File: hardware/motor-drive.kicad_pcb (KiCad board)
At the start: 2 copper layers, 24 parts, among them J1 USB_C_Receptacle_USB2.0_14P, J2 Debug, SW1 RESET, SW2 BOOT, U1 STM32F405RGTx, Y1 8MHz

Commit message: MCU layout
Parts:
- moved C12 38.4 mm to (128.8, 88.0)
- moved R2 37.5 mm to (151.2, 79.6), turned to 180 degrees
- moved C13 36.6 mm to (153.3, 79.6), turned to 180 degrees
- moved J2 35.9 mm to (140.9, 79.7), turned to -90 degrees
- moved L1 35.6 mm to (128.3, 95.7)
- moved C7 35.6 mm to (135.2, 83.9)
- moved C3 34.9 mm to (135.2, 85.0)
- moved C11 33.8 mm to (128.8, 93.5), turned to 180 degrees
- moved Y1 33.1 mm to (128.8, 90.8), turned to -90 degrees
- moved C4 31.7 mm to (144.8, 86.9), turned to 90 degrees
- moved C8 29.3 mm to (145.9, 87.9), turned to 90 degrees
- moved C2 28.3 mm to (129.9, 95.6), turned to -90 degrees
- moved R3 26.5 mm to (147.1, 87.9), turned to 90 degrees
- moved C1 26.2 mm to (131.0, 95.6), turned to -90 degrees
- moved R4 24.3 mm to (147.1, 93.0), turned to -90 degrees
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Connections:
- C13 pad 1: /mcu/BOOT -> +3.3V
- C13 pad 2: GND -> /mcu/BOOT
- C3 pad 1: Net-(C3-Pad1) -> +3.3V
- C4 pad 1: Net-(C3-Pad1) -> +3.3V
- C5 pad 1: Net-(C3-Pad1) -> +3.3V
- C6 pad 1: Net-(C3-Pad1) -> +3.3V
- C7 pad 1: Net-(C3-Pad1) -> +3.3V
- J1 pad A4: VBUS -> unconnected-(J1-VBUS-PadA4)_1
- J1 pad A9: VBUS -> unconnected-(J1-VBUS-PadA4)
- J1 pad B4: VBUS -> unconnected-(J1-VBUS-PadA4)_2
- J1 pad B9: VBUS -> unconnected-(J1-VBUS-PadA4)_3
- J2 pad 1: unconnected-(J2-VTref-Pad1) -> +3.3V
- L1 pad 1: unconnected-(L1-Pad1) -> +3.3V
- R1 pad 1: unconnected-(R1-Pad1) -> +3.3V
- SW2 pad 2: unconnected-(SW2-Pad2) -> +3.3V
- U1 pad 1: Net-(U1-VBAT) -> +3.3V
- U1 pad 13: Net-(U1-VBAT) -> /mcu/VDDA
- U1 pad 19: Net-(U1-VBAT) -> +3.3V
- U1 pad 32: Net-(U1-VBAT) -> +3.3V
- U1 pad 48: Net-(U1-VBAT) -> +3.3V
- U1 pad 64: Net-(U1-VBAT) -> +3.3V
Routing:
- net +3.3V: track 0.00 -> 18.9 mm, vias 0 -> 8
- net /mcu/RESET: track 0.00 -> 17.7 mm, vias 0 -> 2
- net /mcu/SWIO: track 0.00 -> 9.16 mm
- net /USB_DN: track 0.00 -> 7.46 mm
- net /USB_DP: track 0.00 -> 7.38 mm
- net Net-(U1-PH0): track 0.00 -> 7.23 mm
- net /mcu/TDI: track 0.00 -> 6.40 mm, vias 0 -> 2
- net /mcu/SWO: track 0.00 -> 5.86 mm
- net Net-(U1-PH1): track 0.00 -> 5.34 mm
- net /mcu/SWCLK: track 0.00 -> 5.21 mm
- net /mcu/VDDA: track 0.00 -> 4.48 mm
- net /mcu/BOOT: track 0.00 -> 4.32 mm
- net Net-(J1-CC1): track 0.00 -> 2.54 mm
- net Net-(U1-VCAP_2): track 0.00 -> 2.03 mm
- net Net-(J1-CC2): track 0.00 -> 1.94 mm
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- added copper zone on B.Cu, net GND
- added copper zone on F.Cu, net GND
- added copper zone on In1.Cu, net GND
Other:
- copper layers 2 -> 4

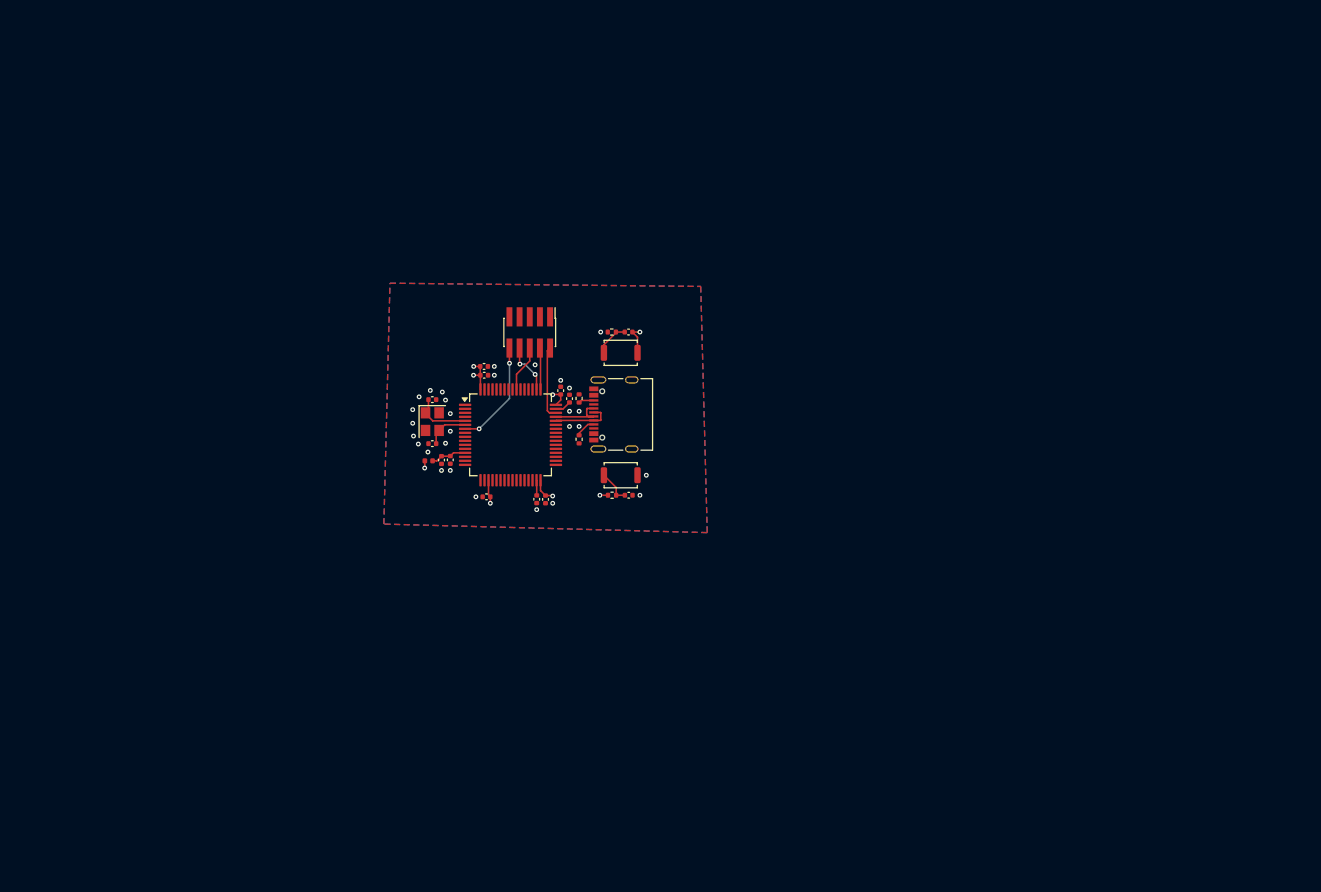
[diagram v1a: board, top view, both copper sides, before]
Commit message: Added power connector
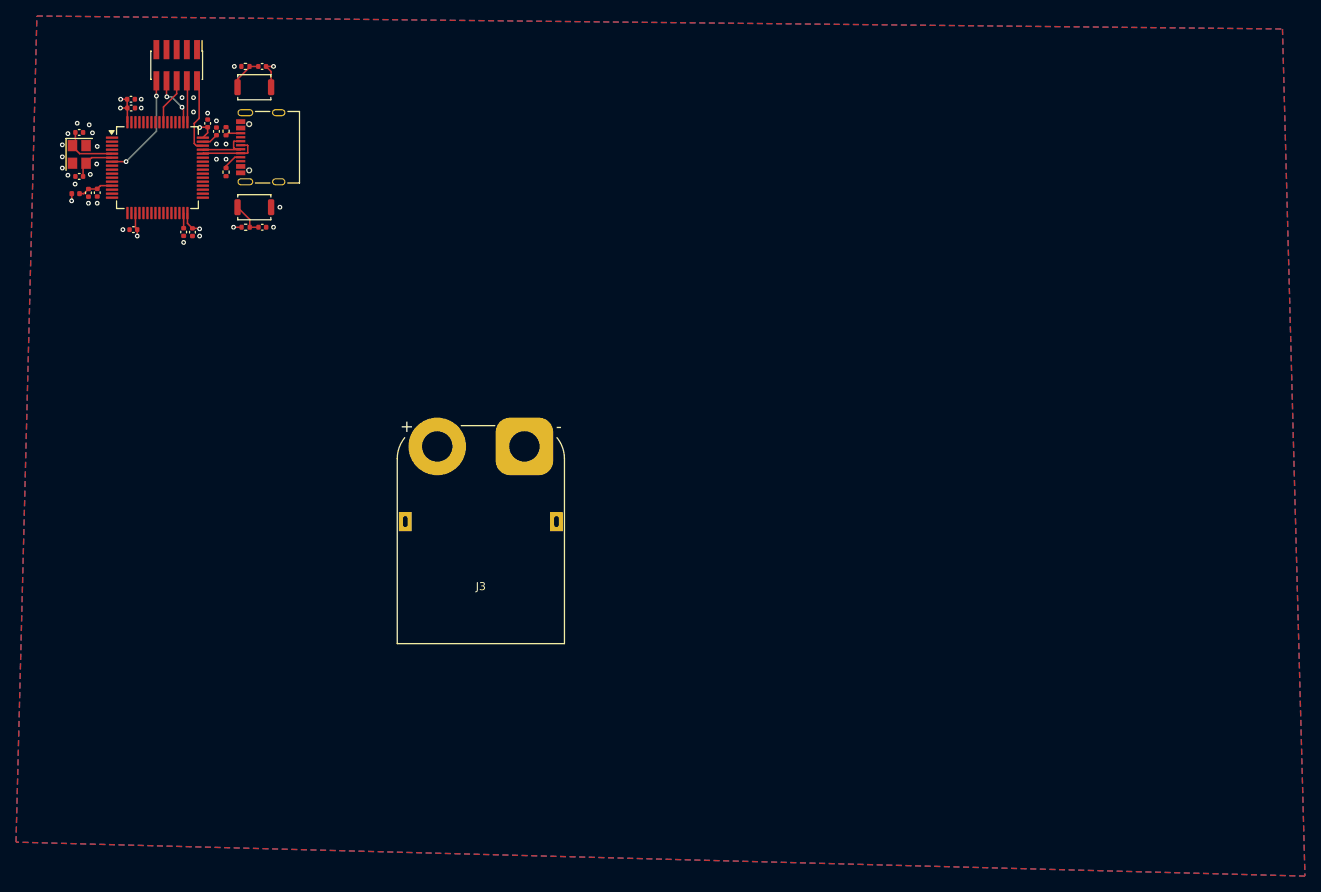
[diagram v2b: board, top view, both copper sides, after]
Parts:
- added J3: BAT, Connector_AMASS:AMASS_XT90PW-M_1x02_P10.90mm_Horizontal, F.Cu at (140.3, 93.9)
- moved C10 56.7 mm to (107.5, 66.5)
- moved SW1 56.7 mm to (106.5, 64.0)
- moved R1 56.7 mm to (105.4, 66.5)
- moved SW2 56.6 mm to (106.5, 49.0)
- moved C13 56.6 mm to (107.5, 46.4)
- moved R2 56.6 mm to (105.4, 46.4)
- moved C3 55.3 mm to (91.1, 51.6)
- moved C4 55.3 mm to (100.7, 53.5)
- moved C6 55.3 mm to (91.4, 66.8)
- moved C9 55.3 mm to (97.7, 67.1)
- moved L1 55.3 mm to (84.2, 62.3)
- moved C7 55.3 mm to (91.1, 50.5)
- moved C8 55.3 mm to (101.8, 54.5)
- moved J1 55.3 mm to (107.3, 56.5)
- moved J2 55.3 mm to (96.8, 46.2)
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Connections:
- J1 pad A8: (no net) -> unconnected-(J1-SBU1-PadA8)
- J1 pad B8: (no net) -> unconnected-(J1-SBU2-PadB8)
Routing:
- net GND: vias 29 -> 31

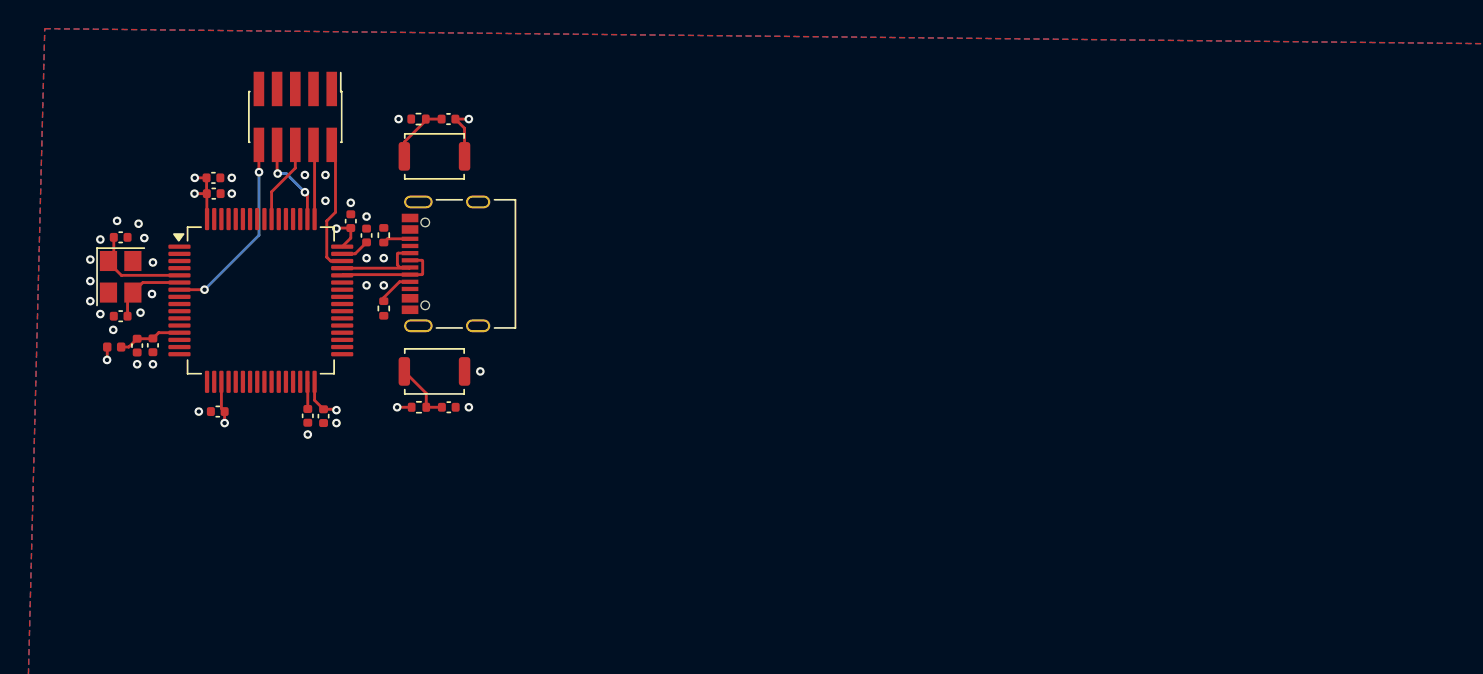
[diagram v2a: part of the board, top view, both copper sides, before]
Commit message: Started work on half bridges
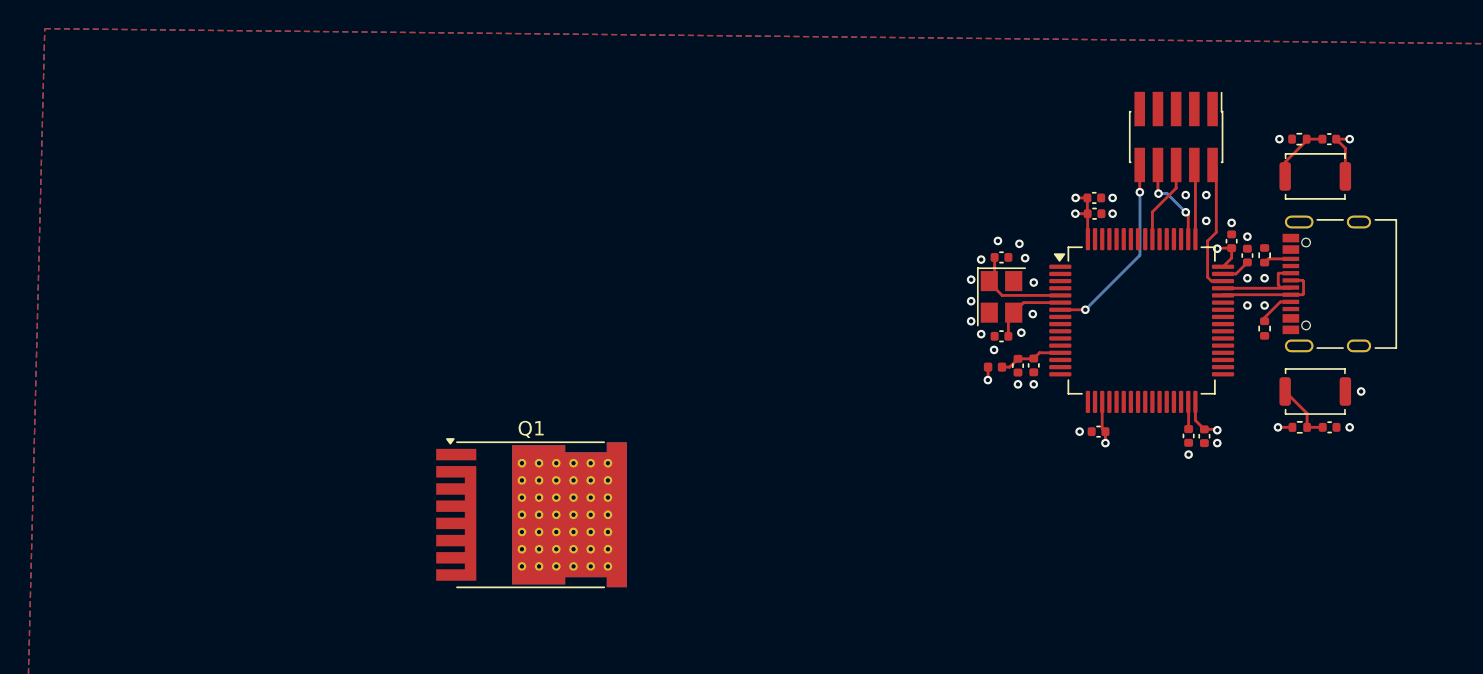
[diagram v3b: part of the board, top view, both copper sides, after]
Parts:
- added Q1: NMOS, Package_TO_SOT_SMD:Infineon_PG-HSOF-8-1_ThermalVias, F.Cu at (113.3, 74.0)
- moved C1 61.4 mm to (148.3, 63.6)
- moved C10 61.4 mm to (168.9, 67.9)
- moved C11 61.4 mm to (146.1, 61.5)
- moved C12 61.4 mm to (146.1, 56.0)
- moved C7 61.4 mm to (152.5, 51.9)
- moved R3 61.4 mm to (164.4, 55.9)
- moved R4 61.4 mm to (164.4, 61.0)
- moved SW1 61.4 mm to (167.9, 65.4)
- moved SW2 61.4 mm to (167.9, 50.4)
- moved Y1 61.4 mm to (146.1, 58.8)
- moved C13 61.4 mm to (168.9, 47.8)
- moved C3 61.4 mm to (152.5, 53.0)
- moved C4 61.4 mm to (162.1, 54.9)
- moved C6 61.4 mm to (152.8, 68.2)
- moved C9 61.4 mm to (159.1, 68.5)
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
